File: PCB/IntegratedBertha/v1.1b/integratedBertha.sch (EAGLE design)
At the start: 97 parts, among them CON1 SPI, IC1 REG1117, IC2 AD8223, J1 RJ12, J2 RJ12, J3 RJ12, J4 RJ12, J5 RJ12, J7 22--02, Q1 BSP75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

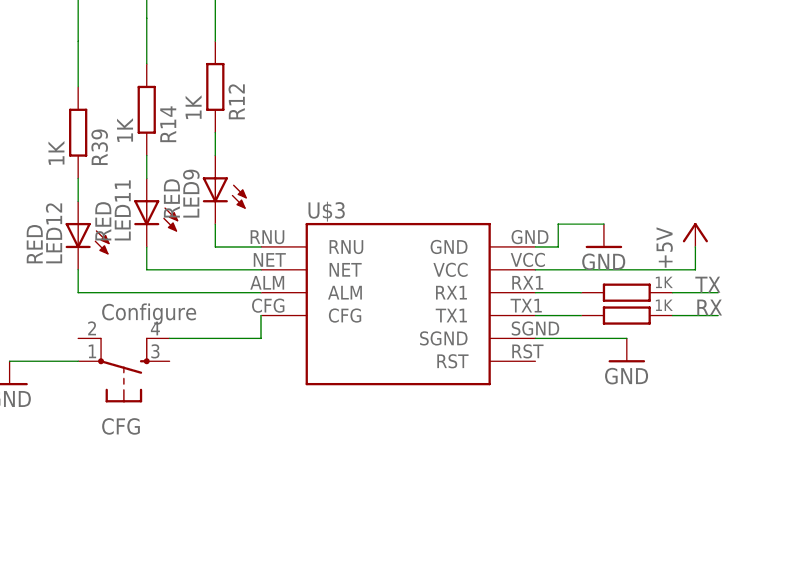
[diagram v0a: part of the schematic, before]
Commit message: added lpatiny.lbr and added throughhole footprint for small zigbee module. CHANGED DESIGN RULES (according to seeedstudios design rules)
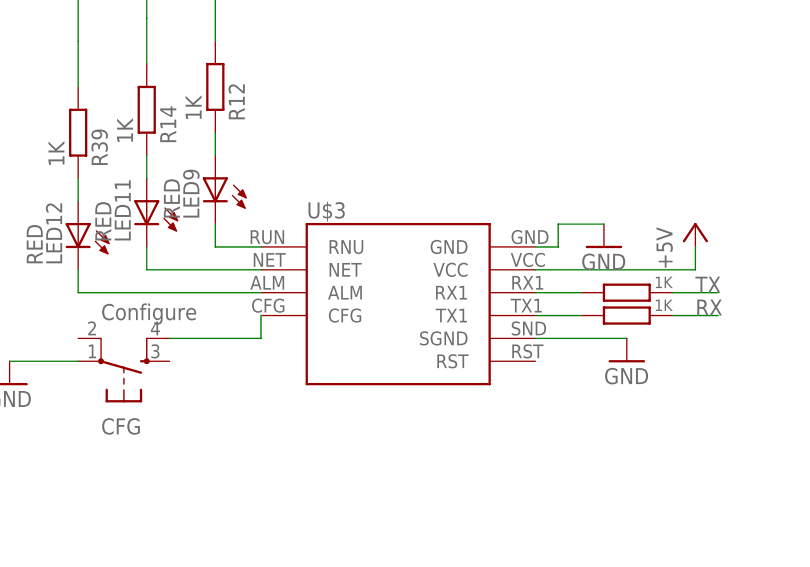
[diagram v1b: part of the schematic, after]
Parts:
- U$3: value SZ05-ZIGBEE -> SZ05-ZIGBEETHROUGHHOLE; device lpatiny:SZ05-ZIGBEE -> lpatiny:SZ05-ZIGBEETHROUGHHOLE
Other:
- moved on the sheet: U$3
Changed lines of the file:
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@@
 <part name="GND8" library="supply1" deviceset="GND" device=""/>
 <part name="GND27" library="supply1" deviceset="GND" device=""/>
-<part name="U$3" library="lpatiny" deviceset="SZ05-ZIGBEE" device="" value="SZ05-ZIGBEE"/>
+<part name="U$3" library="lpatiny" deviceset="SZ05-ZIGBEE" device="THROUGHHOLE" value="SZ05-ZIGBEETHROUGHHOLE"/>
 <part name="R8" library="rcl" deviceset="R-EU_" device="R0805" value="1K"/>
 <part name="R11" library="rcl" deviceset="R-EU_" device="R0805" value="1K"/>
